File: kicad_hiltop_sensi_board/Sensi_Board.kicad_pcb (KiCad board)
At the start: 4 copper layers, 159.9 x 99.9 mm, 331 parts, among them J2 DB44_MALE_MountingHoles, J3 Conn_03x32_DIN41612, J4 RJ45-TRANS_VALCON, J6 Conn_02x08_Odd_Even, K1 HRS1KH-S, Q10 ZXMN6A07F, Q11 ZXMN6A07F, Q2 ZXMN6A07F, Q7 ZXMN6A07F, Q8 ZXMN6A07F, SW1 SW_Push, U1 INA250A4, U13 CP2102N-A01-GQFN24, U14 BTS4140N, U15 BTS4140N, U16 MAX4194, U17 BTS4140N, U18 BTS4140N, U19 MAX4194, U2 LD1117S33TR_SOT223, U20 MAX4194, U21 MAX4194, U22 STM32F072RBTx, U23 MAX4194, U24 MAX4194, U25 MAX4194, U26 MAX4194, U27 USB2502, U3 AT25DN512CSSHF-B, U6 LM75B, Y2 8MHZ, Y3 ABS25-32.768KHZ-6-T

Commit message: Started on Sensi Board Layout
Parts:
- added C24: 100nF, Capacitor_SMD:C_0603_1608Metric, F.Cu at (145.8, 31.6)
- added J1: Conn_01x12, Connector_Molex:Molex_Pico-Clasp_501331-1207_1x12-1MP_P1.00mm_Vertical, F.Cu at (21.9, -56.6)
- added J5: Conn_01x10, Connector_Molex:Molex_Pico-Clasp_501331-1007_1x10-1MP_P1.00mm_Vertical, F.Cu at (130.7, -1.64)
- added J7: Conn_01x12, Connector_Molex:Molex_Pico-Clasp_501331-1207_1x12-1MP_P1.00mm_Vertical, F.Cu at (112.8, 110.1)
- added J8: Conn_01x12, Connector_Molex:Molex_Pico-Clasp_501331-1207_1x12-1MP_P1.00mm_Vertical, F.Cu at (154.2, 110.9)
- added J9: Conn_01x04, Connector_Molex:Molex_Pico-Clasp_501331-0407_1x04-1MP_P1.00mm_Vertical, F.Cu at (71.5, 2.50)
- added JP14: DNF, Connector_PinHeader_1.00mm:PinHeader_1x02_P1.00mm_Vertical, F.Cu at (199.3, 84.7)
- added L1: FB 500mA/0.10DCR, Inductor_SMD:L_0805_2012Metric, F.Cu at (199.6, 88.0)
- added R39: 100K, Resistor_SMD:R_0603_1608Metric, F.Cu at (145.8, 34.1)
- added R40: 100K, Resistor_SMD:R_0603_1608Metric, F.Cu at (149.8, 31.6)
- added SW2: SW_DIP_x04, Button_Switch_SMD:SW_DIP_SPSTx04_Slide_6.7x11.72mm_W6.73mm_P2.54mm_LowProfile_JPin, F.Cu at (101.8, 119.6)
- added SW3: SW_DIP_x04, Button_Switch_SMD:SW_DIP_SPSTx04_Slide_6.7x11.72mm_W6.73mm_P2.54mm_LowProfile_JPin, F.Cu at (143.5, 120.5)
- added SW4: SW_DIP_x04, Button_Switch_SMD:SW_DIP_SPSTx04_Slide_6.7x11.72mm_W6.73mm_P2.54mm_LowProfile_JPin, F.Cu at (164.5, 119.9)
- added SW5: SW_DIP_x04, Button_Switch_SMD:SW_DIP_SPSTx04_Slide_6.7x11.72mm_W6.73mm_P2.54mm_LowProfile_JPin, F.Cu at (121.0, 120.2)
- added U10: MAX31865, Package_DFN_QFN:TQFN-20-1EP_5x5mm_P0.65mm_EP3.1x3.1mm, F.Cu at (101.5, 130.9)
- added U11: MAX31865, Package_DFN_QFN:TQFN-20-1EP_5x5mm_P0.65mm_EP3.1x3.1mm, F.Cu at (120.8, 133.9)
- added U4: AD8646, Package_SO:SOIC-8_3.9x4.9mm_P1.27mm, F.Cu at (13.9, 120.1)
- added U5: AD8646, Package_SO:SOIC-8_3.9x4.9mm_P1.27mm, F.Cu at (5.47, 120.1)
- added U7: AT24C02C-SSHM-T, Package_SO:SOIC-8_3.9x4.9mm_P1.27mm, F.Cu at (199.2, 107.2)
- added U8: MAX31865, Package_DFN_QFN:TQFN-20-1EP_5x5mm_P0.65mm_EP3.1x3.1mm, F.Cu at (144.4, 132.0)
- added U9: MAX31865, Package_DFN_QFN:TQFN-20-1EP_5x5mm_P0.65mm_EP3.1x3.1mm, F.Cu at (164.4, 133.6)
- C55, C56, C60, C61, C66, C67, C79, C82, L11: moved to F.Cu
- J2: value DB44_MALE_MountingHoles -> Conn_01x12; footprint Connector_Dsub:DSUB-44-HD_Female_Horizontal_P2.29x1.98mm_EdgePinOffset8.35mm_Housed_MountingHolesOffset10.89mm -> Connector_Molex:Molex_Pico-Clasp_501331-1207_1x12-1MP_P1.00mm_Vertical
- J4: value RJ45-TRANS_VALCON -> Conn_01x12; footprint Devtank_PCB_Lib:RJ45_TRANSFO_VALCON -> Connector_Molex:Molex_Pico-Clasp_501331-1207_1x12-1MP_P1.00mm_Vertical
- J6: value Conn_02x08_Odd_Even -> Conn_01x10; footprint Connector_IDC:IDC-Header_2x08_P2.54mm_Vertical -> Connector_Molex:Molex_Pico-Clasp_501331-1007_1x10-1MP_P1.00mm_Vertical
- moved TP24 226.4 mm to (36.2, -43.5)
- moved TP18 222.4 mm to (23.4, -33.4)
- moved K1 221.3 mm to (-9.75, -10.7), turned to 0 degrees
- moved TP17 214.5 mm to (37.0, -40.5)
- moved TP16 214.0 mm to (28.1, -31.1)
- moved TP20 209.7 mm to (29.5, -34.1)
- moved TP43 209.3 mm to (20.3, -33.4)
- moved TP15 207.9 mm to (32.5, -34.1)
- moved TP87 207.9 mm to (12.9, -29.9)
- moved D15 206.3 mm to (-4.10, 11.6), turned to 0 degrees
- moved D14 204.3 mm to (-8.55, 16.2), turned to 0 degrees
- moved TP44 203.5 mm to (24.3, -37.3)
- moved R11 202.7 mm to (28.3, -46.5), turned to 0 degrees
- moved TP19 201.6 mm to (34.2, -31.1)
- moved TP45 201.0 mm to (27.8, -40.2)
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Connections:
- C70 pad 2: /TH4- -> /TH4+
- C71 pad 1: /TH4- -> /TH4+
- C71 pad 2: /TH4+ -> /TH4-
- C72 pad 1: /TH4+ -> /TH4-
- J2 pad 1: /GPIO1_EXT -> /GPIO9
- J2 pad 10: /GPIO10_EXT -> GND
- J2 pad 11: /GPIO11_EXT -> (no net)
- J2 pad 12: /PPS1_GPIO12_EXT -> (no net)
- J2 pad 2: /GPIO2_EXT -> GND
- J2 pad 3: /GPIO3_EXT -> /GPIO10
- J2 pad 4: /GPIO4_EXT -> GND
- J2 pad 5: +12V_EXT -> /GPIO11
- J2 pad 6: /OUT1_NC -> /GPIO12
- J2 pad 7: /GPIO7_EXT -> /HS_OUT3
- J2 pad 8: /GPIO8_EXT -> GND
- J2 pad 9: /GPIO9_EXT -> /HS_OUT4
- J3 pad 11a: /FPGA_IO1 -> (no net)
- J3 pad 11b: /SPI0_CS0 -> (no net)
- J3 pad 12a: /FPGA_IO2 -> (no net)
- J3 pad 12b: /SPI0_CS1 -> (no net)
- J3 pad 12c: /I2C0_SDA -> (no net)
- J3 pad 13a: /FPGA_IO3 -> (no net)
- J3 pad 13c: /I2C0_SCL -> (no net)
- J3 pad 14a: /FPGA_IO4 -> (no net)
- J3 pad 14b: /SPI1_MOSI -> (no net)
- J3 pad 15a: /FPGA_IO5 -> (no net)
- J3 pad 15b: /SPI1_MISO -> (no net)
- J3 pad 15c: /I2C1_SDA -> (no net)
- J3 pad 16a: /FPGA_IO6 -> (no net)
- J3 pad 16b: /SPI1_CLK -> (no net)
- J3 pad 16c: /I2C1_SCL -> (no net)
- J3 pad 17a: /FPGA_IO7 -> (no net)
- J3 pad 17b: /SPI1_CS0 -> (no net)
- J3 pad 18a: /FPGA_IO8 -> (no net)
- J3 pad 18b: /SPI1_CS1 -> (no net)
- J3 pad 18c: /MBRD_IO4 -> (no net)
- J3 pad 19a: /FPGA_IO9 -> (no net)
- J3 pad 19b: /SPI1_CS2 -> (no net)
- J3 pad 19c: /MBRD_IO5 -> (no net)
- J3 pad 20a: /FPGA_IO10 -> (no net)
- J3 pad 20b: /GPIO1_MBRD -> (no net)
- J3 pad 20c: /MBRD_IO6 -> (no net)
- J3 pad 21b: /GPIO2_MBRD -> (no net)
- J3 pad 21c: /MBRD_IO7 -> (no net)
- J3 pad 22a: /MBRD_IO8 -> (no net)
- J3 pad 22b: /GPIO3_MBRD -> (no net)
- J3 pad 22c: /PWM0 -> (no net)
- J3 pad 23a: /MBRD_IO9 -> (no net)
- J3 pad 23c: /PWM1 -> (no net)
- J3 pad 24a: /MBRD_IO10 -> (no net)
- J3 pad 24b: /SYS_CLK -> (no net)
- J3 pad 25a: /LCOM_1 -> (no net)
- J3 pad 25b: /SYS_TRIG -> (no net)
- J3 pad 25c: /RCOM_1 -> (no net)
- J3 pad 26a: /LCOM_2 -> (no net)
- J3 pad 26c: /RCOM_2 -> (no net)
- J3 pad 27a: /LCOM_3 -> (no net)
- J3 pad 27b: /SHUTDOWN -> (no net)
- J3 pad 27c: /RCOM_3 -> (no net)
- J3 pad 28a: /LCOM_4 -> (no net)
- J3 pad 28c: /RCOM_4 -> (no net)
- J3 pad 29a: /LCOM_5 -> (no net)
- J3 pad 29c: /RCOM_5 -> (no net)
- J3 pad 2a: /LVDSCLK+ -> (no net)
- J3 pad 30a: /LCOM_6 -> (no net)
- J3 pad 30c: /RCOM_6 -> (no net)
- J3 pad 31a: /LCOM_7 -> (no net)
- J3 pad 31c: /RCOM_7 -> (no net)
- J3 pad 32a: /LCOM_8 -> (no net)
- J3 pad 32c: /RCOM_8 -> (no net)
- J3 pad 3a: /LVDSCLK- -> (no net)
- J3 pad 5a: /LVDS_MOSI+ -> (no net)
- J3 pad 6a: /LVDS_MOSI- -> (no net)
- J3 pad 8a: /LVDS_MISO+ -> (no net)
- J3 pad 9a: /LVDS_MISO- -> (no net)
- J4 pad 1: /TXP -> /TH1+
- J4 pad 10: +3V3 -> /TH4+
- J4 pad 11: Net-(J4-Pad11) -> /TH4-
- J4 pad 12: +3V3 -> GND
- J4 pad 2: /TXN -> /TH1-
- J4 pad 3: Net-(C6-Pad2) -> GND
- J4 pad 4: Earth -> /TH2+
- J4 pad 5: Earth -> /TH2-
- J4 pad 6: Net-(C6-Pad2) -> GND
- J4 pad 7: /RXP -> /TH3+
- J4 pad 8: /RXN -> /TH3-
- J4 pad 9: Net-(J4-Pad9) -> GND
- J6 pad 1: +12V_EXT -> /F3+
- J6 pad 10: /OUT5_COM -> (no net)
- J6 pad 2: /OUT1_COM -> /F3-
- J6 pad 3: /OUT1_NC -> GND
- J6 pad 4: /OUT4_COM -> /F2+
- J6 pad 5: /OUT2_COM -> /F2-
- J6 pad 6: /OUT4_NO -> GND
- J6 pad 7: /OUT2_NO -> /F4+
- J6 pad 8: /OUT4_NC -> /F4-
- J6 pad 9: /OUT2_NC -> GND
- R70 pad 2: /TH4+ -> /TH4-
- U13 pad 1: Net-(U13-Pad1) -> (no net)
- U13 pad 10: Net-(U13-Pad10) -> (no net)
- U13 pad 15: Net-(U13-Pad15) -> (no net)
- U13 pad 16: Net-(U13-Pad16) -> (no net)
- U13 pad 17: Net-(U13-Pad17) -> (no net)
- U13 pad 18: Net-(U13-Pad18) -> (no net)
- U13 pad 19: Net-(U13-Pad19) -> (no net)
- U13 pad 22: Net-(U13-Pad22) -> (no net)
- U13 pad 23: Net-(U13-Pad23) -> (no net)
- U13 pad 24: Net-(U13-Pad24) -> (no net)
- U22 pad 1: Net-(U22-Pad1) -> (no net)
- U22 pad 33: Net-(U22-Pad33) -> Net-(R121-Pad2)
- U22 pad 36: Net-(U22-Pad36) -> /HS_CTRL_SW4
- U22 pad 37: Net-(U22-Pad37) -> (no net)
- U22 pad 46: Net-(R121-Pad2) -> /SWD_IO
- U22 pad 49: /HS_CTRL_SW4 -> /SWD_SCK
- U22 pad 51: /STM_Micro/DUT1_UART_RX_GPIO15 -> (no net)
- U22 pad 52: /STM_Micro/DUT1_UART_TX_GPIO16 -> (no net)
- U25 pad 2: /TH4+ -> /TH4-
- U25 pad 3: /TH4- -> /TH4+
- U27 pad 11: Net-(U27-Pad11) -> (no net)
- U27 pad 12: Net-(U27-Pad12) -> (no net)
- U27 pad 14: Net-(U27-Pad14) -> (no net)
- U27 pad 15: Net-(U27-Pad15) -> (no net)
- U27 pad 23: Net-(U27-Pad23) -> (no net)
- U6 pad 3: Net-(U6-Pad3) -> (no net)
- Y2 pad 2: Net-(Y2-Pad2) -> (no net)
- Y2 pad 4: Net-(Y2-Pad4) -> (no net)
- Y3 pad 2: Net-(Y3-Pad2) -> (no net)
- Y3 pad 3: Net-(Y3-Pad3) -> (no net)
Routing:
- net /GPIO8: track 234.0 -> 0.00 mm, vias 3 -> 0
- net GND: track 222.2 -> 0.00 mm, vias 215 -> 0
- net /GPIO1_EXT: track 177.1 -> 0.00 mm
- net /GPIO2_EXT: track 172.1 -> 0.00 mm, vias 1 -> 0
- net /GPIO11: track 161.9 -> 0.00 mm, vias 3 -> 0
- net +5V: track 160.3 -> 0.00 mm, vias 5 -> 0
- net /GPIO9: track 154.2 -> 0.00 mm, vias 3 -> 0
- net /12V_ADC8: track 145.2 -> 0.00 mm, vias 1 -> 0
- net /DUT1_UART_TX_GPIO16: track 139.4 -> 0.00 mm, vias 2 -> 0
- net /12V_ADC9: track 138.5 -> 0.00 mm, vias 1 -> 0
- net /USB_DATA_N: track 133.7 -> 0.00 mm
- net /12V_ADC10: track 132.4 -> 0.00 mm, vias 1 -> 0
- net /USB_DATA_P: track 132.2 -> 0.00 mm
- net /5V_ADC7: track 128.1 -> 0.00 mm
- net /3V3_ADC3: track 124.1 -> 0.00 mm
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- removed copper zone on In2.Cu, net +12V
- removed copper zone on In2.Cu, net +3V3
- removed copper zone on In2.Cu, net +5V
- removed copper zone on In2.Cu, net ADJ_DC
- removed copper zone on B.Cu, net Earth
- removed copper zone on F.Cu, net Earth
- removed copper zone on In1.Cu, net Earth
- removed copper zone on In2.Cu, net Earth
- removed copper zone on B.Cu, net GND
- removed copper zone on F.Cu, net GND
- removed copper zone on In1.Cu, net GND
- removed copper zone on F.Cu, net Net-(F1-Pad1)
- removed copper zone on F.Cu, net Net-(R11-Pad2)
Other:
- board text removed: "LoTI Board PN: 304-006 Rev: A"
- board text removed: "S/N:"

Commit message: Updated board layout LBBC sensi board
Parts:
- removed J9: Conn_01x04, Connector_Molex:Molex_Pico-Clasp_501331-0407_1x04-1MP_P1.00mm_Vertical
- added D1: B240A-13, Diode_SMD:D_SMA, F.Cu at (101.3, 61.7)
- added J10: Conn_ARM_JTAG_SWD_10, Connector_PinHeader_2.54mm:PinHeader_2x05_P2.54mm_Vertical, F.Cu at (179.3, 159.9)
- C96: moved to B.Cu
- J1, J2, J4, J7, J8: value Conn_01x12 -> Conn_02x06_Counter_Clockwise; footprint Connector_Molex:Molex_Pico-Clasp_501331-1207_1x12-1MP_P1.00mm_Vertical -> Devtank_PCB_Lib:Molex2x06
- J5, J6: value Conn_01x10 -> Conn_02x06_Counter_Clockwise; footprint Connector_Molex:Molex_Pico-Clasp_501331-1007_1x10-1MP_P1.00mm_Vertical -> Devtank_PCB_Lib:Molex2x06
- R69: value R -> 100R 0.1%
- SW2, SW3, SW4, SW5: footprint Button_Switch_SMD:SW_DIP_SPSTx04_Slide_6.7x11.72mm_W6.73mm_P2.54mm_LowProfile_JPin -> Button_Switch_SMD:SW_DIP_SPSTx04_Slide_Copal_CHS-04B_W7.62mm_P1.27mm
- moved C25 279.8 mm to (270.6, 92.5), turned to 180 degrees
- moved TP4 276.4 mm to (273.7, 101.5)
- moved R18 272.5 mm to (263.2, 95.2), turned to 90 degrees
- moved R35 269.9 mm to (267.0, 92.5), turned to 180 degrees
- moved R19 267.8 mm to (263.2, 98.9), turned to 90 degrees
- moved D14 263.2 mm to (253.9, -3.45), turned to 270 degrees
- moved TP3 258.0 mm to (258.5, 95.8)
- moved U4 255.9 mm to (268.8, 97.0)
- moved D16 253.6 mm to (248.3, -3.35), turned to 270 degrees
- moved C21 253.4 mm to (276.7, 93.8)
- moved R28 249.4 mm to (276.7, 97.2)
- moved R125 245.4 mm to (253.9, -0.35)
- moved C14 243.9 mm to (274.3, 93.7)
- moved R24 241.5 mm to (270.5, 101.5), turned to 0 degrees
- moved R126 240.5 mm to (248.2, 0.05)
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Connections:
- C101 pad 1: +5V_ISO1 -> +3V3
- C102 pad 1: +5V_ISO1 -> +3V3
- C103 pad 1: +5V_ISO1 -> +3V3
- C105 pad 1: +5V_ISO1 -> +3V3
- C106 pad 1: +5V_ISO1 -> +3V3
- C23 pad 1: +5V_ISO1 -> +3V3
- C24 pad 1: +5V_ISO1 -> +3V3
- C40 pad 2: +5V_ISO1 -> +3V3
- C41 pad 2: +5V_ISO1 -> +3V3
- C48 pad 2: +5V_ISO1 -> +3V3
- C49 pad 2: +5V_ISO1 -> +3V3
- C68 pad 2: +5V_ISO1 -> +3V3
- C69 pad 2: +5V_ISO1 -> +3V3
- C86 pad 2: +5V_ISO1 -> +3V3
- C87 pad 2: +5V_ISO1 -> +3V3
- C96 pad 1: +5V_ISO1 -> +3V3
- C97 pad 1: +5V_ISO1 -> +3V3
- C98 pad 1: +5V_ISO1 -> +3V3
- J4 pad 10: /TH4+ -> /TH3-
- J4 pad 11: /TH4- -> /TH3+
- J4 pad 7: /TH3+ -> /TH4-
- J4 pad 8: /TH3- -> /TH4+
- J6 pad 1: /F3+ -> /F1+
- J6 pad 10: (no net) -> /F3-
- J6 pad 2: /F3- -> /F1-
- J6 pad 7: /F4+ -> /F4-
- J6 pad 8: /F4- -> /F4+
- J7 pad 1: /RTD1_F+ -> /RTD3_F+
- J7 pad 10: GND -> /RTD4_R-
- J7 pad 11: (no net) -> GND
- J7 pad 2: /RTD1_F- -> /RTD3_F-
- J7 pad 3: /RTD1_R+ -> /RTD3_R+
- J7 pad 4: /RTD1_R- -> /RTD3_R-
- J7 pad 6: /RTD2_F+ -> (no net)
- J7 pad 7: /RTD2_F- -> /RTD4_F+
- J7 pad 8: /RTD2_R+ -> /RTD4_F-
- J7 pad 9: /RTD2_R- -> /RTD4_R+
- J8 pad 1: /RTD3_F+ -> /RTD1_F+
- J8 pad 10: GND -> /RTD2_R-
- J8 pad 11: (no net) -> GND
- J8 pad 2: /RTD3_F- -> /RTD1_F-
- J8 pad 3: /RTD3_R+ -> /RTD1_R+
- J8 pad 4: /RTD3_R- -> /RTD1_R-
- J8 pad 6: /RTD4_F+ -> (no net)
- J8 pad 7: /RTD4_F- -> /RTD2_F+
- J8 pad 8: /RTD4_R+ -> /RTD2_F-
- J8 pad 9: /RTD4_R- -> /RTD2_R+
- R105 pad 2: +5V_ISO1 -> +3V3
- R110 pad 2: +5V_ISO1 -> +3V3
- R112 pad 1: +5V_ISO1 -> +3V3
- R30 pad 1: +5V_ISO1 -> +3V3
- R32 pad 1: +5V_ISO1 -> +3V3
- R34 pad 1: +5V_ISO1 -> +3V3
- R37 pad 1: +5V_ISO1 -> +3V3
- R38 pad 1: +5V_ISO1 -> +3V3
- R40 pad 2: +5V_ISO1 -> +3V3
- R74 pad 1: +5V_ISO1 -> +3V3
- R90 pad 1: +5V_ISO1 -> +3V3
- R93 pad 1: +5V_ISO1 -> +3V3
- U16 pad 7: +5V_ISO1 -> +3V3
- U19 pad 7: +5V_ISO1 -> +3V3
- U20 pad 7: +5V_ISO1 -> +3V3
- U21 pad 7: +5V_ISO1 -> +3V3
- U23 pad 7: +5V_ISO1 -> +3V3
- U24 pad 7: +5V_ISO1 -> +3V3
- U25 pad 7: +5V_ISO1 -> +3V3
- U26 pad 7: +5V_ISO1 -> +3V3
- U27 pad 1: +5V_ISO1 -> +3V3
- U27 pad 13: +5V_ISO1 -> +3V3
- U27 pad 28: +5V_ISO1 -> +3V3
- U27 pad 33: +5V_ISO1 -> +3V3
- U27 pad 34: +5V_ISO1 -> +3V3
- U27 pad 7: +5V_ISO1 -> +3V3
- U6 pad 8: +5V_ISO1 -> +3V3
- U7 pad 8: +5V_ISO1 -> +3V3

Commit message: Updated sensi board layout LBBC
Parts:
- added Y1: 50ppm 24.000MHZ, Crystal:Crystal_SMD_TXC_7A-2Pin_5x3.2mm, F.Cu at (85.8, 79.4)
- C1: footprint Capacitor_SMD:C_0603_1608Metric -> Crystal:Crystal_SMD_TXC_7A-2Pin_5x3.2mm
- J5: moved to B.Cu
- moved C69 205.4 mm to (165.4, 86.0), turned to 270 degrees
- moved R9 202.6 mm to (195.6, 135.3), turned to 180 degrees
- moved R48 200.1 mm to (183.9, 138.7), turned to 180 degrees
- moved R10 198.7 mm to (195.6, 132.3), turned to 180 degrees
- moved D2 198.5 mm to (180.6, 138.7), turned to 0 degrees
- moved R61 196.4 mm to (194.1, 50.2), turned to 90 degrees
- moved R60 195.8 mm to (192.3, 50.2), turned to 90 degrees
- moved D4 195.7 mm to (174.8, 138.4), turned to 0 degrees
- moved R50 195.5 mm to (184.8, 134.8), turned to 90 degrees
- moved R8 195.2 mm to (195.7, 129.6), turned to 180 degrees
- moved U24 195.0 mm to (171.1, 86.6), turned to 180 degrees
- moved R52 194.6 mm to (182.9, 134.8), turned to 270 degrees
- moved R53 193.5 mm to (185.2, 50.3), turned to 90 degrees
- moved R51 193.1 mm to (183.4, 50.3), turned to 270 degrees
- moved Q2 193.0 mm to (180.1, 134.8), turned to 180 degrees
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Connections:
- J1 pad 1: /HS_OUT1 -> /GPIO5
- J1 pad 10: /GPIO6 -> /HS_OUT1
- J1 pad 11: /GPIO7 -> /GPIO3
- J1 pad 12: /GPIO8 -> /GPIO4
- J1 pad 2: GND -> /GPIO6
- J1 pad 3: /HS_OUT2 -> /GPIO7
- J1 pad 4: GND -> /GPIO8
- J1 pad 7: /GPIO3 -> /HS_OUT2
- J1 pad 8: /GPIO4 -> GND
- J1 pad 9: /GPIO5 -> GND
- J2 pad 1: /GPIO9 -> (no net)
- J2 pad 10: GND -> /GPIO9
- J2 pad 11: (no net) -> GND
- J2 pad 12: (no net) -> /HS_OUT3
- J2 pad 3: /GPIO10 -> (no net)
- J2 pad 5: /GPIO11 -> GND
- J2 pad 6: /GPIO12 -> /HS_OUT4
- J2 pad 7: /HS_OUT3 -> /GPIO12
- J2 pad 8: GND -> /GPIO11
- J2 pad 9: /HS_OUT4 -> /GPIO10
- J5 pad 11: (no net) -> GND
- J5 pad 12: (no net) -> /ADC12
- J5 pad 7: /ADC12 -> (no net)
- J5 pad 8: GND -> (no net)
- U16 pad 6: /ADC5 -> /ADC8
- U19 pad 6: /ADC7 -> /ADC6
- U20 pad 6: /ADC6 -> /ADC5
- U21 pad 6: /ADC8 -> /ADC7
- U22 pad 10: /ADC10 -> /ADC2
- U22 pad 11: /ADC11 -> /ADC1
- U22 pad 14: /ADC1 -> /ADC5
- U22 pad 15: /ADC2 -> /ADC6
- U22 pad 16: /STM_DEBUG_TX -> /ADC7
- U22 pad 17: /STM_DEBUG_RX -> /ADC8
- U22 pad 2: /GPIO6 -> /GPIO11
- U22 pad 20: /ADC3 -> /ADC9
- U22 pad 22: /ADC4 -> /ADC10
- U22 pad 23: /ADC5 -> /ADC11
- U22 pad 26: /ADC6 -> /STM_RES2
- U22 pad 27: /ADC7 -> /GPIO12
- U22 pad 28: /GPIO8 -> /GPIO3
- U22 pad 29: /GPIO5 -> /STM_DEBUG_TX
- U22 pad 30: /STM_RES2 -> /STM_DEBUG_RX
- U22 pad 33: Net-(R121-Pad2) -> /HS_CTRL_SW2
- U22 pad 34: /STM_SCL -> /GPIO5
- U22 pad 35: /STM_SDA -> /GPIO6
- U22 pad 36: /HS_CTRL_SW4 -> /GPIO7
- U22 pad 38: /GPIO12 -> /GPIO8
- U22 pad 39: /RL1_OUT -> /GPIO1
- U22 pad 41: /GPIO4 -> /GPIO2
- U22 pad 42: /HS_CTRL_SW1 -> /GPIO4
- U22 pad 43: /HS_CTRL_SW2 -> /HS_CTRL_SW1
- U22 pad 50: /GPIO2 -> /HS_CTRL_SW4
- U22 pad 51: (no net) -> Net-(R121-Pad2)
- U22 pad 53: /GPIO1 -> (no net)
- U22 pad 54: /GPIO7 -> /RL1_OUT
- U22 pad 58: /GPIO10 -> /STM_SCL
- U22 pad 59: /GPIO3 -> /STM_SDA
- U22 pad 62: /GPIO11 -> /GPIO10
- U22 pad 8: /ADC8 -> /ADC4
- U22 pad 9: /ADC9 -> /ADC3

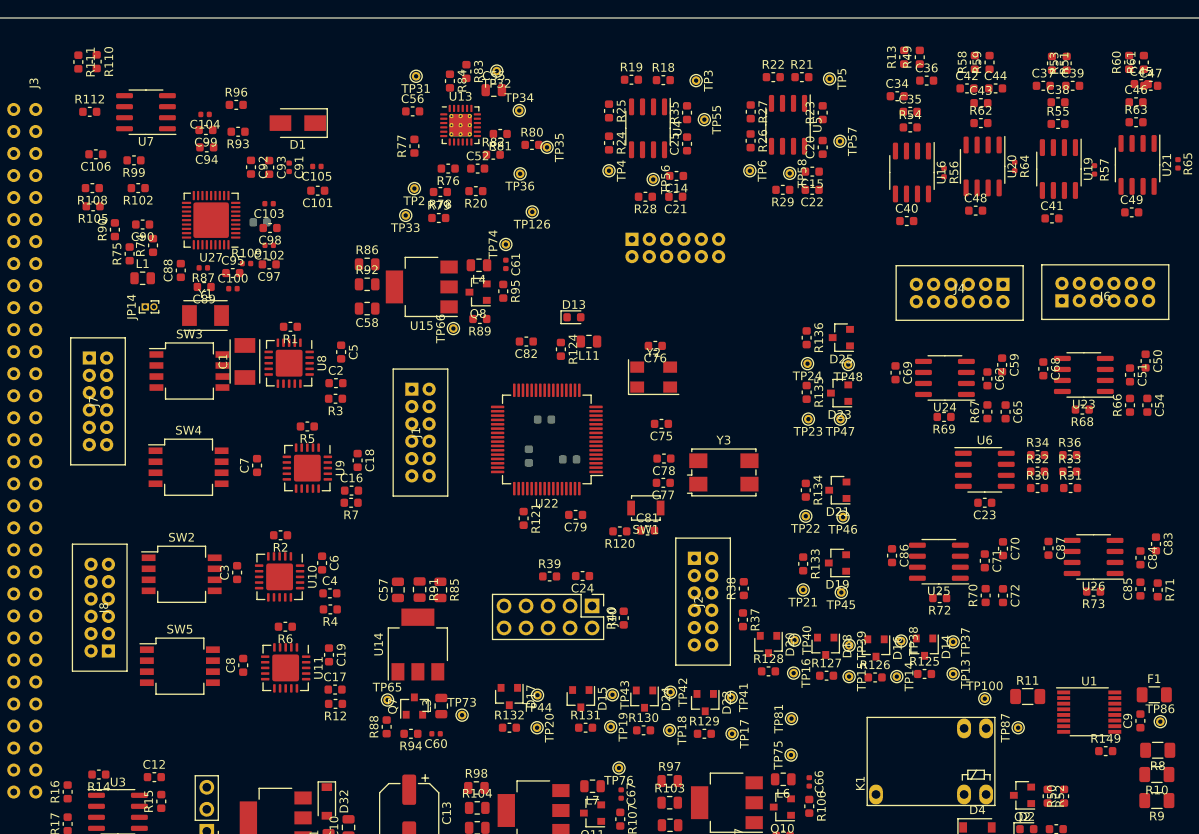
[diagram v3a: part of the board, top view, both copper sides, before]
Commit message: Sensi board updated pin map
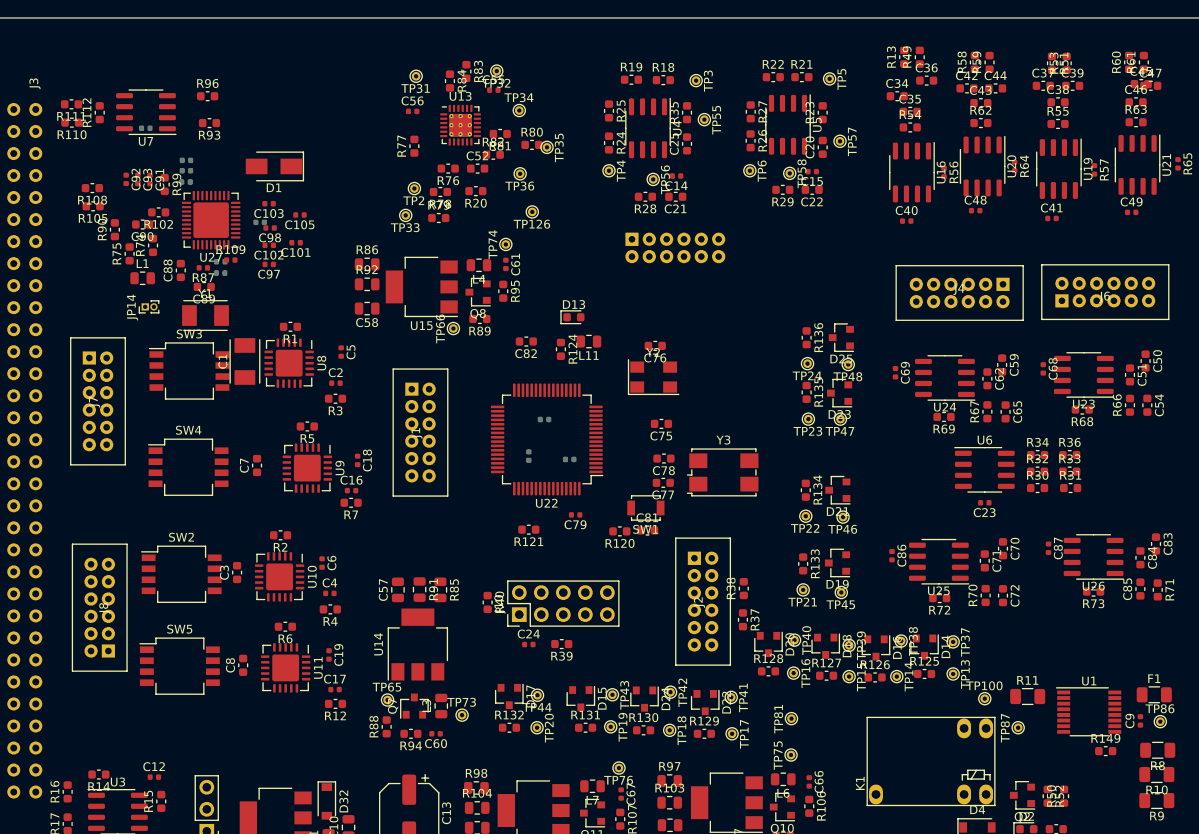
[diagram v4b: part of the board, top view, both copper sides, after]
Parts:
- C100, C104: moved to B.Cu
- C101, C12, C14, C15, C16, C17, C18, C19, C2, C23, C24, C4, C40, C41, C48, C49, C5, C56, C6, C68, C69, C73, C74, C79, C80, C86, C87, C9, C92, C93, C96, C97, C98: footprint Capacitor_SMD:C_0603_1608Metric -> Capacitor_SMD:C_0402_1005Metric
- C106, C94, C95, C99: footprint Capacitor_SMD:C_0603_1608Metric -> Capacitor_SMD:C_0402_1005Metric; moved to B.Cu
- C55: footprint Capacitor_SMD:C_0805_2012Metric -> Capacitor_SMD:C_0402_1005Metric
- moved C91 16.1 mm to (79.4, 63.7)
- moved R40 15.8 mm to (118.3, 112.5), turned to 270 degrees
- moved C93 15.2 mm to (78.0, 63.7)
- moved C92 14.5 mm to (76.7, 63.7)
- moved C24 10.0 mm to (123.1, 117.3), turned to 0 degrees
- moved J10 8.46 mm to (122.0, 113.9), turned to 90 degrees
- moved C104 8.10 mm to (83.5, 64.0)
- moved R39 7.92 mm to (126.9, 117.3), turned to 180 degrees
- moved R110 7.60 mm to (70.4, 57.1), turned to 180 degrees
- moved C101 6.50 mm to (96.2, 71.0)
- moved C106 6.50 mm to (78.9, 57.8), turned to 0 degrees
- moved C105 5.93 mm to (96.7, 67.8)
- moved D1 5.71 mm to (93.7, 62.2)
- moved C99 5.21 mm to (83.6, 62.7)
- moved R111 4.94 mm to (70.3, 55.0), turned to 180 degrees
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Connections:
- U20 pad 6: /ADC5 -> /ADC7
- U21 pad 6: /ADC7 -> /ADC5
- U22 pad 10: /ADC2 -> /ADC3
- U22 pad 11: /ADC1 -> /ADC2
- U22 pad 14: /ADC5 -> /ADC1
- U22 pad 15: /ADC6 -> /GPIO12
- U22 pad 16: /ADC7 -> /ADC5
- U22 pad 17: /ADC8 -> /ADC6
- U22 pad 20: /ADC9 -> /ADC7
- U22 pad 22: /ADC10 -> /ADC8
- U22 pad 23: /ADC11 -> /ADC12
- U22 pad 24: /ADC12 -> /ADC11
- U22 pad 25: /STM_Micro/ADC13 -> /ADC10
- U22 pad 27: /GPIO12 -> /ADC9
- U22 pad 54: /RL1_OUT -> /GPIO9
- U22 pad 61: /GPIO9 -> /GPIO10
- U22 pad 62: /GPIO10 -> /RL1_OUT
- U22 pad 8: /ADC4 -> /STM_Micro/ADC13
- U22 pad 9: /ADC3 -> /ADC4
- U23 pad 6: /ADC1 -> /ADC2
- U24 pad 6: /ADC3 -> /ADC1
- U26 pad 6: /ADC2 -> /ADC3
